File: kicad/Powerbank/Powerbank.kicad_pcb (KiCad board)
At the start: 2 copper layers, 90 x 60 mm, 141 parts, among them IC1 BQ4050RSMR, IC4 BQ25703ARSNT, IC5 TPD6S300ARUKR, IC6 W25Q80DVSNIG, J1 USB_C_Receptacle, J2 USB_A

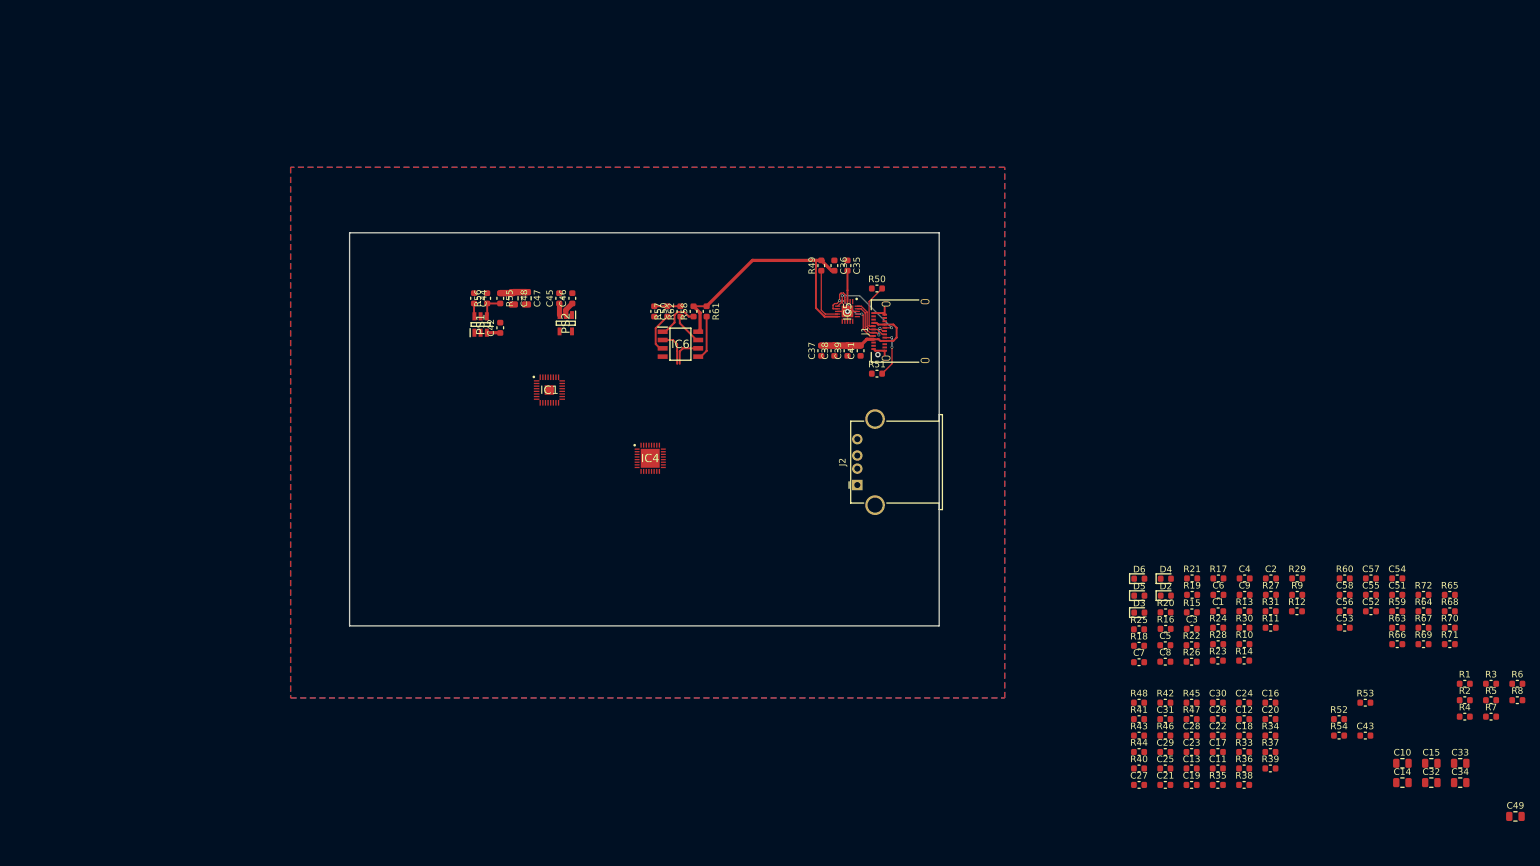
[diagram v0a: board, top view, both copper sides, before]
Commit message: Added footprint for all, moved to a first attempt for routing
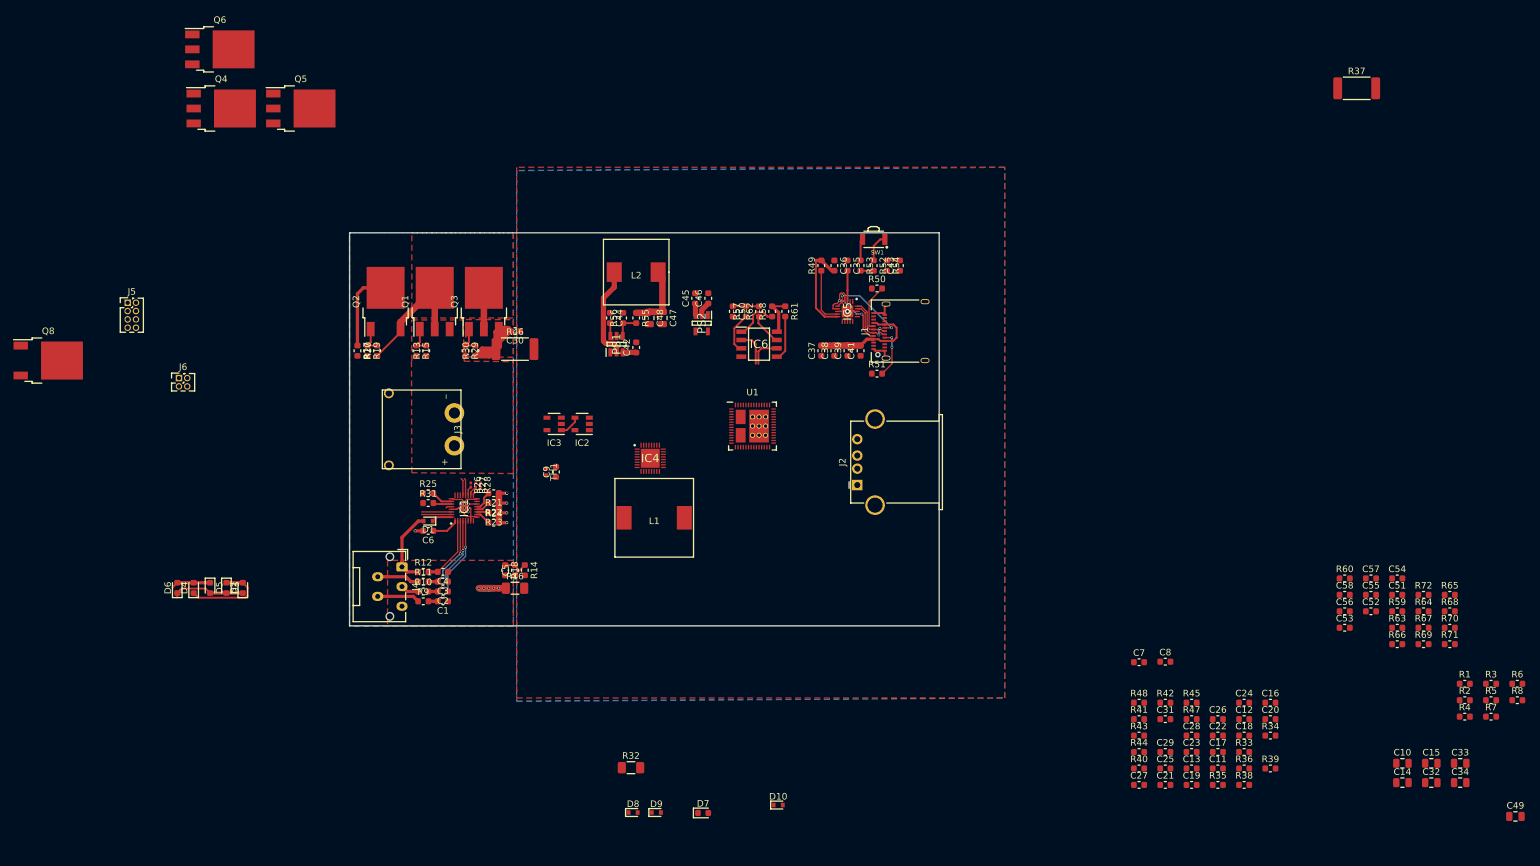
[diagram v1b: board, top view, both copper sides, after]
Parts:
- added D1: D_Schottky, Diode_SMD:D_SOD-523, F.Cu at (112.0, 114.0)
- added D10: D_Schottky, Diode_SMD:D_SOD-523, F.Cu at (165.4, 157.3)
- added D7: D_Schottky, Diode_SMD:D_0603_1608Metric, F.Cu at (154.0, 158.6)
- added D8: D_Schottky, Diode_SMD:D_SOD-523, F.Cu at (143.3, 158.5)
- added D9: D_Schottky, Diode_SMD:D_SOD-523, F.Cu at (146.8, 158.5)
- added IC2: SN74LVC1G14DSFR, Package_TO_SOT_SMD:SOT-23-5, F.Cu at (135.5, 99.2)
- added IC3: SN74LVC1G08DSFR, Package_TO_SOT_SMD:SOT-23-5, F.Cu at (131.2, 99.2)
- added J3: Conn_01x02_Male, Powerbank:XT30PW-M, F.Cu at (116.0, 100.0)
- added J4: Conn_01x05_Male, Connector_JST:JST_ZE_S05B-ZESK-2D_1x05_P1.50mm_Horizontal, F.Cu at (108.0, 121.0)
- added J5: Conn_01x08_Male, Connector_PinHeader_1.27mm:PinHeader_2x04_P1.27mm_Vertical, F.Cu at (66.1, 80.7)
- added J6: Conn_01x04_Male, Connector_PinHeader_1.27mm:PinHeader_2x02_P1.27mm_Vertical, F.Cu at (74.0, 92.2)
- added L1: 2.2µH, Powerbank:WE_Inductor_7443330220, F.Cu at (146.5, 113.5)
- added L2: 3.3µH, Powerbank:WE_Inductor_8070_7443340330, F.Cu at (143.8, 76.0)
- added Q1: Q_NMOS_GDS, Package_TO_SOT_SMD:TO-252-3_TabPin2, F.Cu at (113.0, 80.5)
- added Q2: Q_PMOS_GDS, Package_TO_SOT_SMD:TO-252-2, F.Cu at (105.5, 80.5)
- added Q3: Q_NMOS_GDS, Package_TO_SOT_SMD:TO-252-3_TabPin2, F.Cu at (120.5, 80.5)
- added Q4: Q_NMOS_GDS, Package_TO_SOT_SMD:TO-252-3_TabPin2, F.Cu at (80.4, 51.0)
- added Q5: Q_NMOS_GDS, Package_TO_SOT_SMD:TO-252-3_TabPin2, F.Cu at (92.6, 51.0)
- added Q6: Q_NMOS_GDS, Package_TO_SOT_SMD:TO-252-3_TabPin2, F.Cu at (80.2, 42.0)
- added Q8: Q_PMOS_GDS, Package_TO_SOT_SMD:TO-252-2, F.Cu at (54.0, 89.5)
- added R32: 2.2R, Resistor_SMD:R_1206_3216Metric, F.Cu at (143.0, 151.6)
- added SW1: SW_DIP_x01, Powerbank:SW_B3U-3000P, F.Cu at (180.0, 71.0)
- added TH1: 10k, Resistor_SMD:R_0402_1005Metric, F.Cu at (130.0, 106.5)
- added U1: TPS65988DH, Powerbank:QFN-56_7x7_Pitch0.4mm, F.Cu at (161.5, 99.5)
- R16: footprint Resistor_SMD:R_0603_1608Metric -> Resistor_SMD:R_1206_3216Metric
- R26, R27, R28: footprint Resistor_SMD:R_0603_1608Metric -> Resistor_SMD:R_0201_0603Metric
- R37: footprint Resistor_SMD:R_0603_1608Metric -> Resistor_SMD:R_2512_6332Metric
- R46: value R01 -> 0.01R; footprint Resistor_SMD:R_0603_1608Metric -> Resistor_SMD:R_2512_6332Metric
- moved D4 148.4 mm to (76.2, 124.2), turned to 90 degrees
- moved D6 146.9 mm to (73.7, 124.2), turned to 90 degrees
- moved D5 141.8 mm to (78.7, 124.2), turned to 270 degrees
- moved D2 140.9 mm to (83.7, 124.2), turned to 90 degrees
- moved D3 139.4 mm to (81.2, 124.2), turned to 270 degrees
- moved R17 135.9 mm to (101.2, 88.0), turned to 270 degrees
- moved R12 133.5 mm to (111.2, 121.8)
- moved R9 133.4 mm to (111.2, 126.2)
- moved R29 131.6 mm to (117.7, 88.0), turned to 270 degrees
- moved R19 131.3 mm to (102.7, 88.0), turned to 270 degrees
- moved R13 131.1 mm to (111.7, 88.0), turned to 90 degrees
- moved R31 129.7 mm to (112.0, 111.2)
- moved R11 129.5 mm to (111.2, 123.2)
- moved R20 126.8 mm to (104.2, 88.0), turned to 90 degrees
- moved C2 126.4 mm to (114.2, 124.8), turned to 180 degrees
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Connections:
- R20 pad 1: Net-(Q1-Pad1) (its old number) -> /Cell Balancer BQ4050/Source
- R25 pad 1: Net-(Q1-Pad1) (its old number) -> /Cell Balancer BQ4050/Source
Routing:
- net -BATT: track 0.00 -> 32.8 mm, vias 0 -> 20
- net /Cell Balancer BQ4050/Source: track 0.00 -> 26.6 mm
- net +VDC: track 0.00 -> 21.9 mm
- net PD_LDO_3V3: track 41.0 -> 21.4 mm
- net Net-(D2-Pad2): track 0.00 -> 16.1 mm
- net Net-(C1-Pad2): track 0.00 -> 15.5 mm, vias 0 -> 2
- net Net-(L2-Pad1): track 0.00 -> 14.4 mm
- net Net-(D2-Pad1): track 0.00 -> 14.0 mm
- net Net-(C2-Pad2): track 0.00 -> 13.8 mm, vias 0 -> 2
- net Net-(Q2-Pad2): track 0.00 -> 12.6 mm
- net Net-(C3-Pad2): track 0.00 -> 12.2 mm, vias 0 -> 2
- net CELL4: track 0.00 -> 11.6 mm
- net Net-(C4-Pad2): track 0.00 -> 10.5 mm
- net CELL3: track 0.00 -> 6.47 mm
- net CELL1: track 0.00 -> 6.47 mm
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- added copper zone on F.Cu, net +VDC
- added copper zone on B.Cu, net -BATT
- added copper zone on F.Cu, net -BATT
- added copper zone on F.Cu, net /Cell Balancer BQ4050/Source
- added copper zone on F.Cu, net CELL4

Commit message: Added more routing
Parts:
- moved R70 158.2 mm to (111.8, 155.8)
- moved R72 154.9 mm to (111.8, 154.2)
- moved R71 154.7 mm to (114.8, 154.2)
- moved C34 153.5 mm to (145.5, 63.5), turned to 180 degrees
- moved C49 152.6 mm to (125.8, 147.5), turned to 90 degrees
- moved R69 150.9 mm to (114.8, 155.8)
- moved C33 150.6 mm to (145.5, 65.5), turned to 180 degrees
- moved C54 149.6 mm to (114.8, 158.8), turned to 180 degrees
- moved C32 147.6 mm to (145.5, 67.5), turned to 180 degrees
- moved C51 147.2 mm to (114.8, 149.8), turned to 180 degrees
- moved R68 144.4 mm to (126.2, 155.5), turned to 180 degrees
- moved C57 144.3 mm to (114.8, 152.8), turned to 180 degrees
- moved C52 144.2 mm to (114.8, 157.2), turned to 180 degrees
- moved R67 141.0 mm to (124.0, 147.5), turned to 270 degrees
- moved C53 138.7 mm to (114.8, 151.2), turned to 180 degrees
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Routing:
- net TP1: track 0.00 -> 36.1 mm
- net TP2: track 0.00 -> 12.4 mm
- net Net-(C5-Pad1): track 2.20 -> 12.4 mm
- net Net-(C5-Pad2): track 1.50 -> 11.0 mm, vias 0 -> 2
- net SPI_CSZ: track 6.91 -> 15.7 mm, vias 0 -> 2
- net SPI_MOSI: track 6.89 -> 15.2 mm
- net ADCIN2: track 0.00 -> 7.00 mm
- net SW_SIG: track 0.00 -> 6.78 mm
- net ADCIN1: track 0.00 -> 6.46 mm
- net SYS: track 6.39 -> 12.7 mm
- net Net-(IC6-Pad3): track 6.26 -> 0.00 mm
- net VBUS_A: track 0.00 -> 5.07 mm
- net PP_HV: track 0.00 -> 4.47 mm
- net SPI_MISO: track 5.48 -> 9.88 mm, vias 0 -> 2
- net SPI_CLK: track 4.90 -> 9.30 mm
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- added copper zone on F.Cu, net Net-(C27-Pad2)
- added copper zone on F.Cu, net SYS
- removed copper zone on F.Cu, net GND

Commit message: Routed some of components of battery charger
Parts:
- moved R65 151.0 mm to (120.8, 159.0), turned to 90 degrees
- moved R64 148.0 mm to (119.2, 159.0), turned to 90 degrees
- moved R63 145.0 mm to (117.8, 159.0), turned to 90 degrees
- moved C55 137.8 mm to (122.2, 159.0), turned to 270 degrees
- moved C56 131.9 mm to (123.8, 159.0), turned to 270 degrees
- moved C20 114.2 mm to (133.8, 103.8), turned to 180 degrees
- moved R36 112.8 mm to (133.8, 105.2), turned to 180 degrees
- moved R39 112.6 mm to (136.8, 108.2)
- moved R38 111.9 mm to (136.8, 103.8)
- moved C19 109.0 mm to (131.5, 104.5), turned to 90 degrees
- moved C24 103.4 mm to (137.5, 112.0), turned to 90 degrees
- moved C22 102.7 mm to (136.8, 109.8), turned to 180 degrees
- moved R33 101.9 mm to (141.8, 112.0), turned to 270 degrees
- moved R34 101.5 mm to (145.5, 111.2)
- moved C21 100.5 mm to (136.8, 105.2), turned to 180 degrees
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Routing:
- net VDDA: track 0.00 -> 10.9 mm, vias 0 -> 2
- net GND: track 15.1 -> 25.4 mm, vias 7 -> 22
- net ACN: track 0.00 -> 8.24 mm
- net Net-(IC4-Pad20): track 0.00 -> 6.87 mm
- net Net-(IC4-Pad19): track 0.00 -> 6.83 mm
- net Net-(IC4-Pad18): track 0.00 -> 6.08 mm
- net Net-(C22-Pad1): track 0.00 -> 5.48 mm
- net SCL_1: track 0.00 -> 5.37 mm
- net TP3: track 0.00 -> 5.19 mm
- net Net-(IC4-Pad6): track 0.00 -> 5.17 mm
- net Net-(C27-Pad2): track 0.00 -> 5.16 mm
- net SNK_EVENT: track 0.00 -> 4.96 mm
- net SDA_1: track 0.00 -> 4.74 mm
- net Net-(C23-Pad2): track 0.00 -> 4.54 mm
- net TP4: track 0.00 -> 4.51 mm
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
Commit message: Updated routing
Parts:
- added Q7: Q_NMOS_GDS, Package_TO_SOT_SMD:TO-252-3_TabPin2, F.Cu at (144.5, 80.5)
- C12: footprint Capacitor_SMD:C_0603_1608Metric -> Capacitor_SMD:C_0805_2012Metric
- moved C15 132.6 mm to (165.2, 63.8), turned to 180 degrees
- moved C14 129.9 mm to (165.2, 65.8), turned to 180 degrees
- moved C10 127.2 mm to (171.8, 60.0)
- moved C18 112.1 mm to (130.8, 109.8)
- moved C12 104.6 mm to (165.2, 67.8), turned to 180 degrees
- moved R32 103.9 mm to (167.8, 60.0), turned to 180 degrees
- moved R37 93.1 mm to (161.5, 60.8)
- moved R47 88.4 mm to (148.5, 106.8), turned to 180 degrees
- moved C28 87.8 mm to (150.8, 106.0), turned to 90 degrees
- moved R44 84.4 mm to (148.5, 105.2), turned to 180 degrees
- moved R35 49.4 mm to (130.8, 108.2)
- moved Q4 7.00 mm to (158.5, 80.5)
- moved Q5 7.00 mm to (151.5, 80.5)
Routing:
- net PP_HV: track 4.47 -> 48.4 mm, vias 0 -> 2
- net +VDC: track 21.9 -> 60.2 mm, vias 0 -> 2
- net Net-(C27-Pad2): track 5.16 -> 38.6 mm, vias 0 -> 2
- net Net-(IC4-Pad21): track 2.08 -> 35.2 mm, vias 0 -> 2
- net TP6: track 1.95 -> 28.9 mm, vias 0 -> 2
- net TP2: track 14.5 -> 37.9 mm, vias 0 -> 2
- net Net-(C26-Pad1): track 4.36 -> 21.6 mm
- net Net-(C25-Pad1): track 2.61 -> 19.5 mm, vias 0 -> 4
- net TP1: track 39.0 -> 23.5 mm, vias 0 -> 2
- net TP5: track 2.39 -> 13.7 mm, vias 0 -> 3
- net ACP: track 2.56 -> 11.0 mm
- net TP3: track 5.19 -> 9.40 mm, vias 0 -> 2
- net SYS: track 14.7 -> 18.3 mm
- net Net-(IC4-Pad19): track 6.83 -> 5.20 mm
- net Net-(IC4-Pad20): track 6.87 -> 6.17 mm

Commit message: Updated routing
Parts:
- moved J5 120.3 mm to (176.5, 128.5), turned to 90 degrees
- moved J6 114.4 mm to (182.8, 127.2)
- moved C46 82.5 mm to (153.5, 129.0), turned to 0 degrees
- moved C45 80.5 mm to (153.5, 127.0), turned to 0 degrees
- moved L2 79.6 mm to (157.0, 120.8), turned to 270 degrees
- moved R72 77.9 mm to (168.4, 100.8), turned to 270 degrees
- moved R70 77.9 mm to (166.9, 100.8), turned to 270 degrees
- moved PS2 77.8 mm to (149.7, 128.0), turned to 180 degrees
- moved C47 75.3 mm to (150.0, 124.8), turned to 180 degrees
- moved C51 74.1 mm to (172.9, 103.8), turned to 90 degrees
- moved C53 73.9 mm to (171.4, 103.8), turned to 90 degrees
- moved C57 73.8 mm to (169.9, 103.8), turned to 90 degrees
- moved R71 73.7 mm to (168.4, 103.8), turned to 270 degrees
- moved R69 73.6 mm to (166.9, 103.8), turned to 270 degrees
- moved C48 73.5 mm to (150.0, 122.8), turned to 180 degrees
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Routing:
- net GND: track 25.4 -> 61.5 mm, vias 22 -> 46
- net DP_C: track 8.31 -> 42.3 mm, vias 2 -> 4
- net DN_C: track 7.26 -> 39.5 mm, vias 0 -> 2
- net VBUS_C: track 21.2 -> 43.5 mm
- net TP1: track 23.5 -> 42.7 mm
- net TP2: track 37.9 -> 52.5 mm
- net DN_A: track 0.00 -> 12.8 mm
- net TP3: track 9.40 -> 21.9 mm
- net TP5: track 13.7 -> 26.1 mm
- net TP4: track 4.51 -> 15.7 mm
- net PP_HV: track 48.4 -> 40.4 mm, vias 2 -> 10
- net +5V: track 12.2 -> 20.2 mm
- net DP_A: track 0.00 -> 7.81 mm
- net DRAIN2: track 0.00 -> 6.44 mm
- net PD_LDO_3V3: track 25.4 -> 18.9 mm
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- added copper zone on F.Cu, net Net-(C20-Pad1)

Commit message: First routing finished, correcting DRC warnings
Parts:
- moved R8 132.6 mm to (149.2, 110.5), turned to 90 degrees
- moved R3 126.7 mm to (150.8, 110.5), turned to 90 degrees
- moved R7 126.5 mm to (152.2, 110.5), turned to 90 degrees
- moved R6 124.5 mm to (155.5, 118.2), turned to 180 degrees
- moved R5 121.3 mm to (155.5, 116.8), turned to 180 degrees
- moved C8 114.1 mm to (119.2, 91.5), turned to 90 degrees
- moved R1 113.8 mm to (158.5, 117.2)
- moved C7 111.8 mm to (117.8, 91.5), turned to 270 degrees
- moved R2 110.6 mm to (162.2, 117.2), turned to 180 degrees
- moved R4 99.1 mm to (173.8, 121.0), turned to 180 degrees
- moved D8 78.3 mm to (186.0, 74.2), turned to 180 degrees
- moved D9 75.7 mm to (186.1, 75.8), turned to 180 degrees
- moved D7 70.3 mm to (183.5, 78.5)
- moved D6 70.3 mm to (120.8, 72.0), turned to 270 degrees
- moved D4 67.0 mm to (118.3, 72.0), turned to 270 degrees
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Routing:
- net SCL_1: track 5.37 -> 143.2 mm, vias 0 -> 8
- net SYS: track 17.4 -> 152.3 mm, vias 0 -> 13
- net SDA_1: track 4.74 -> 134.7 mm, vias 0 -> 4
- net SYS_EN: track 1.50 -> 99.0 mm, vias 0 -> 2
- net PD_LDO_3V3: track 18.9 -> 116.2 mm, vias 0 -> 11
- net SW: track 3.71 -> 96.1 mm, vias 0 -> 4
- net GND: track 61.5 -> 150.9 mm, vias 46 -> 79
- net CC1: track 2.05 -> 73.4 mm, vias 0 -> 5
- net +3V3: track 3.49 -> 72.4 mm, vias 0 -> 2
- net CC2: track 2.51 -> 66.2 mm, vias 0 -> 2
- net SRC_EVT: track 0.00 -> 59.6 mm, vias 0 -> 2
- net PP_HV: track 40.4 -> 94.9 mm
- net PROCHOT: track 1.91 -> 44.0 mm, vias 0 -> 3
- net Net-(D4-Pad2): track 6.03 -> 47.5 mm, vias 0 -> 2
- net Net-(C20-Pad1): track 2.93 -> 43.9 mm, vias 0 -> 2
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- added copper zone on GND.Cu, net -BATT
- added copper zone on POWER.Cu, net CELL4
- added copper zone on GND.Cu, net GND
- removed copper zone on B.Cu, net -BATT
- removed copper zone on B.Cu, net GND
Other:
- copper layers 2 -> 4
- rule trace_min: 0.2 -> 0.1
- rule via_min_size: 0.4 -> 0.5
- board text added: "B+"
- board text added: "B-"
- board text added: "MOSI|MISO CS|CLK"
- board text added: "Powerbank USB-C PD Oskar Johansson 2020-01"
- board text added: "SDA|CC2|GPIO13|GND SCL|CC1|GPIO12|3V3"
